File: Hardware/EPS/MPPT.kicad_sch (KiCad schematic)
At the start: 34 parts

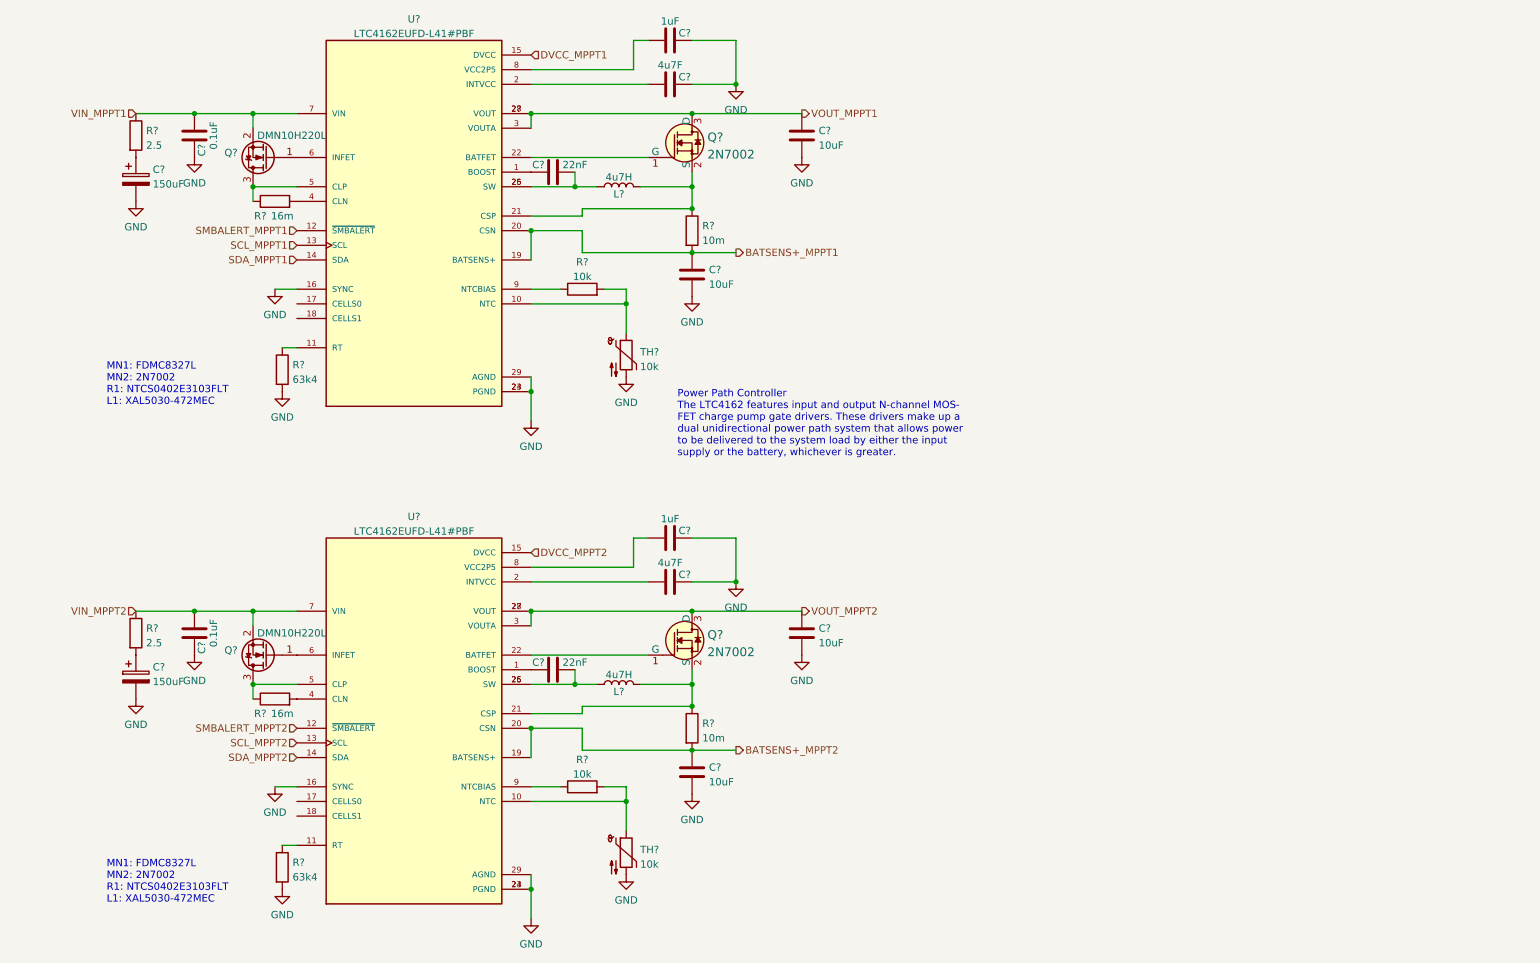
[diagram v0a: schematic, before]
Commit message: Added USB, Solar Connector and MATLAB Folder
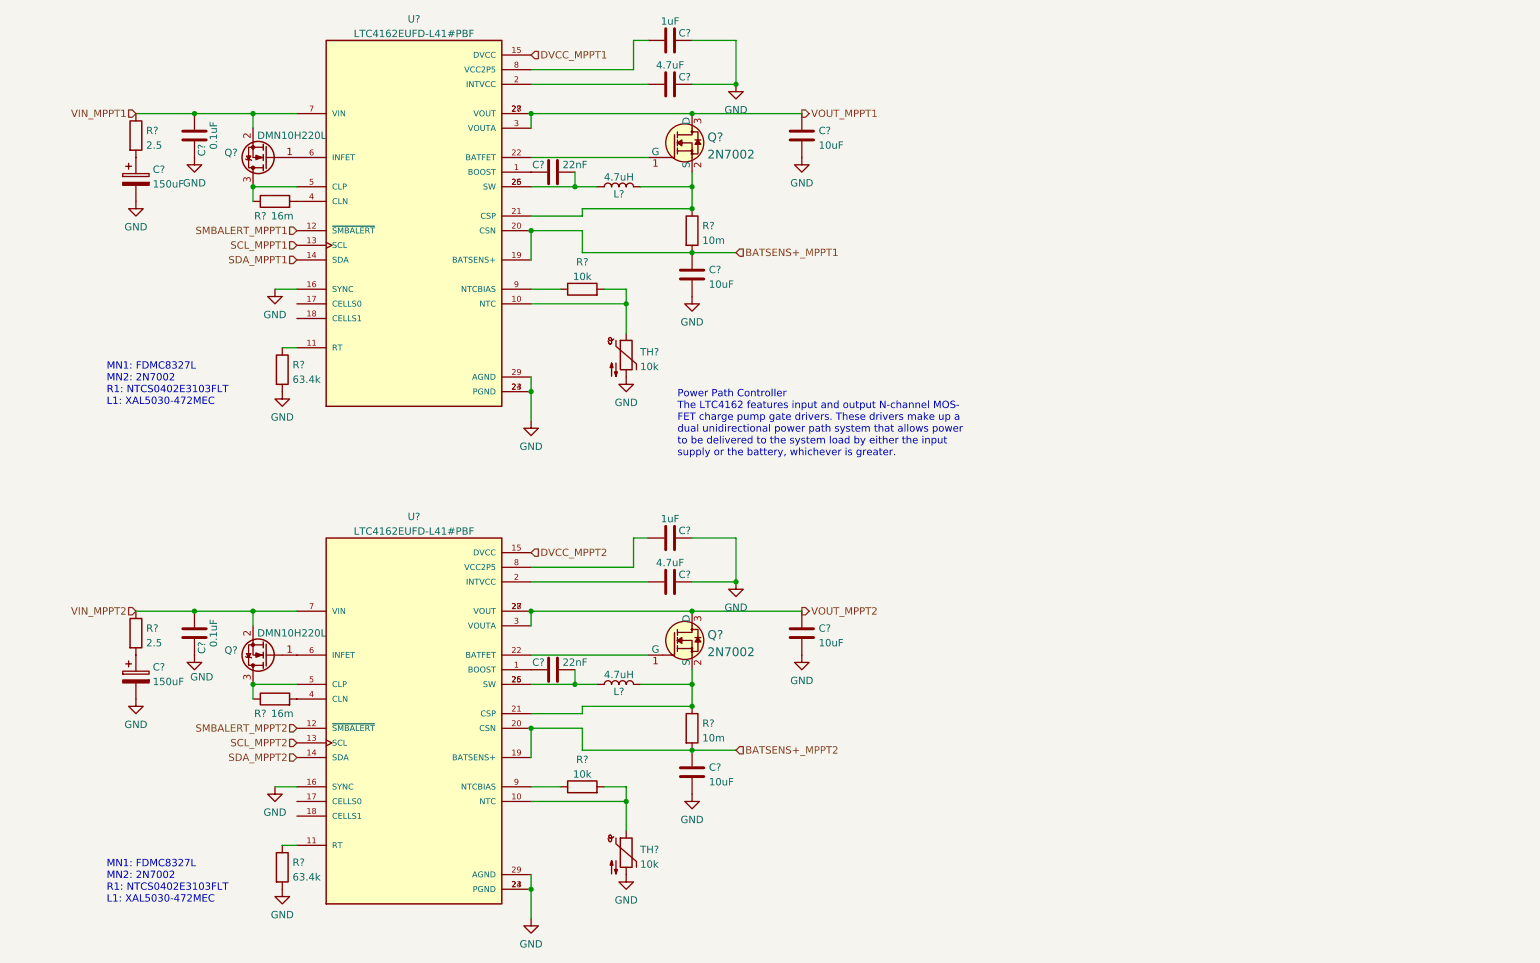
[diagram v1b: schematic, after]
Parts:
- C? (x2): value 4u7F -> 4.7uF
- L? (x2): value 4u7H -> 4.7uH
- R? (x2): value 63k4 -> 63.4k
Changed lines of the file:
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@@
     (effects (font (size 1.27 1.27)) (justify right))
   )
-  (hierarchical_label "BATSENS+_MPPT2" (shape output) (at 144.78 144.78 0)
+  (hierarchical_label "BATSENS+_MPPT2" (shape input) (at 144.78 144.78 0)
     (effects (font (size 1.27 1.27)) (justify left))
   )
@@
     (effects (font (size 1.27 1.27)) (justify right))
   )
-  (hierarchical_label "BATSENS+_MPPT1" (shape output) (at 144.78 58.42 0)
+  (hierarchical_label "BATSENS+_MPPT1" (shape input) (at 144.78 58.42 0)
     (effects (font (size 1.27 1.27)) (justify left))
   )
@@
   )
   (symbol (lib_id "power:GND") (at 50.8 128.27 0) (unit 1)
-    (in_bom yes) (on_board yes) (fields_autoplaced)
+    (in_bom yes) (on_board yes)
     (property "Reference" "#PWR?" (id 0) (at 50.8 134.62 0)
       (effects (font (size 1.27 1.27)) hide)
     )
-    (property "Value" "GND" (id 1) (at 50.8 132.7134 0))
+    (property "Value" "GND" (id 1) (at 52.07 132.08 0))
     (property "Footprint" "" (id 2) (at 50.8 128.27 0)
       (effects (font (size 1.27 1.27)) hide)
@@
     (in_bom yes) (on_board yes)
     (property "Reference" "C?" (id 0) (at 135.89 27.94 90))
-    (property "Value" "4u7F" (id 1) (at 133.35 25.8881 90))
+    (property "Value" "4.7uF" (id 1) (at 133.35 25.8881 90))
     (property "Footprint" "" (id 2) (at 137.16 28.2448 0)
       (effects (font (size 1.27 1.27)) hide)
@@
       (effects (font (size 1.27 1.27)) (justify left))
     )
-    (property "Value" "63k4" (id 1) (at 67.818 166.8022 0)
+    (property "Value" "63.4k" (id 1) (at 67.818 166.8022 0)
       (effects (font (size 1.27 1.27)) (justify left))
     )
@@
       (effects (font (size 1.27 1.27)) (justify left))
     )
-    (property "Value" "63k4" (id 1) (at 67.818 80.4422 0)
+    (property "Value" "63.4k" (id 1) (at 67.818 80.4422 0)
       (effects (font (size 1.27 1.27)) (justify left))
     )
@@
     (in_bom yes) (on_board yes)
     (property "Reference" "L?" (id 0) (at 124.46 134.62 90))
-    (property "Value" "4u7H" (id 1) (at 124.46 131.6791 90))
+    (property "Value" "4.7uH" (id 1) (at 124.46 131.6791 90))
     (property "Footprint" "" (id 2) (at 124.46 133.35 0)
       (effects (font (size 1.27 1.27)) hide)
@@
     (in_bom yes) (on_board yes)
     (property "Reference" "L?" (id 0) (at 124.46 48.26 90))
-    (property "Value" "4u7H" (id 1) (at 124.46 45.3191 90))
+    (property "Value" "4.7uH" (id 1) (at 124.46 45.3191 90))
     (property "Footprint" "" (id 2) (at 124.46 46.99 0)
       (effects (font (size 1.27 1.27)) hide)
@@
     (in_bom yes) (on_board yes)
     (property "Reference" "C?" (id 0) (at 135.89 114.3 90))
-    (property "Value" "4u7F" (id 1) (at 133.35 112.2481 90))
+    (property "Value" "4.7uF" (id 1) (at 133.35 112.2481 90))
     (property "Footprint" "" (id 2) (at 137.16 114.6048 0)
       (effects (font (size 1.27 1.27)) hide)

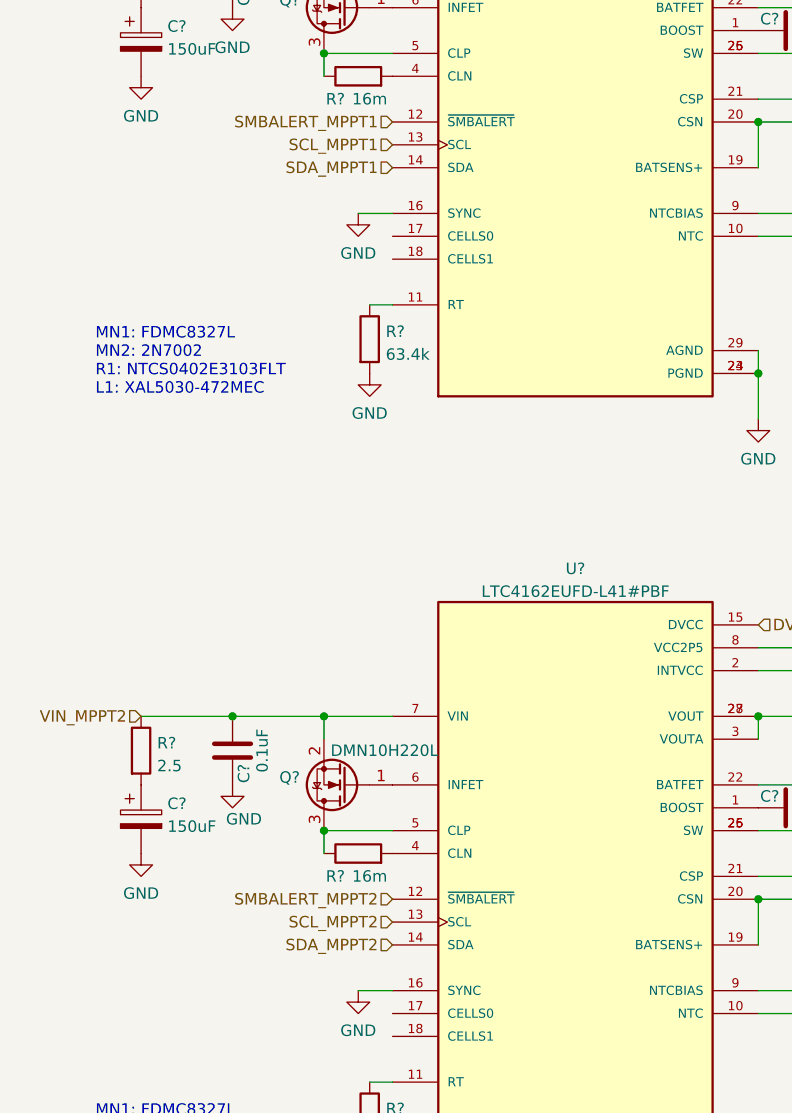
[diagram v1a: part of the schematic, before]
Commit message: Added interboard connector and MCU
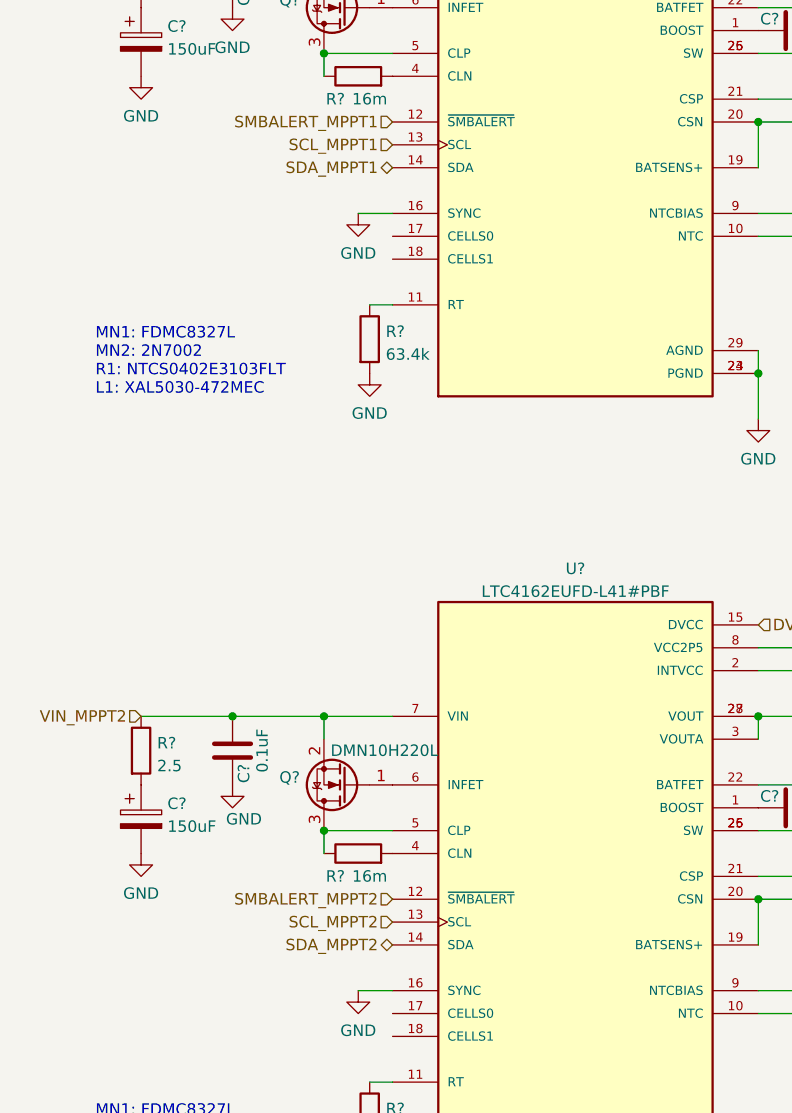
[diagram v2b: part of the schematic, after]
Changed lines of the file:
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@@
     (effects (font (size 1.27 1.27)) (justify left bottom))
   )
-  (hierarchical_label "SDA_MPPT2" (shape input) (at 68.58 146.05 180)
+  (hierarchical_label "SDA_MPPT2" (shape bidirectional) (at 68.58 146.05 180)
     (effects (font (size 1.27 1.27)) (justify right))
   )
@@
     (effects (font (size 1.27 1.27)) (justify right))
   )
-  (hierarchical_label "SDA_MPPT1" (shape input) (at 68.58 59.69 180)
+  (hierarchical_label "SDA_MPPT1" (shape bidirectional) (at 68.58 59.69 180)
     (effects (font (size 1.27 1.27)) (justify right))
   )

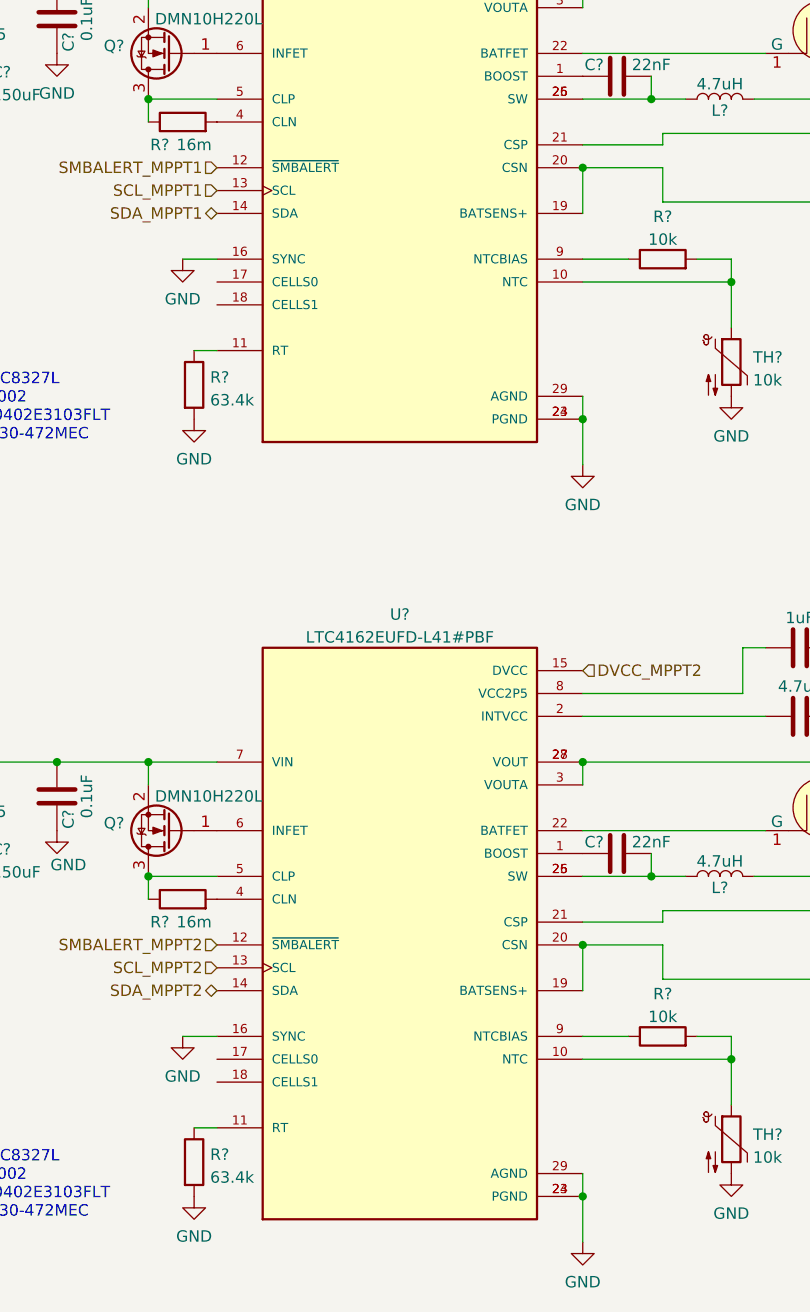
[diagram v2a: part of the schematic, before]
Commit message: Added board connector layout
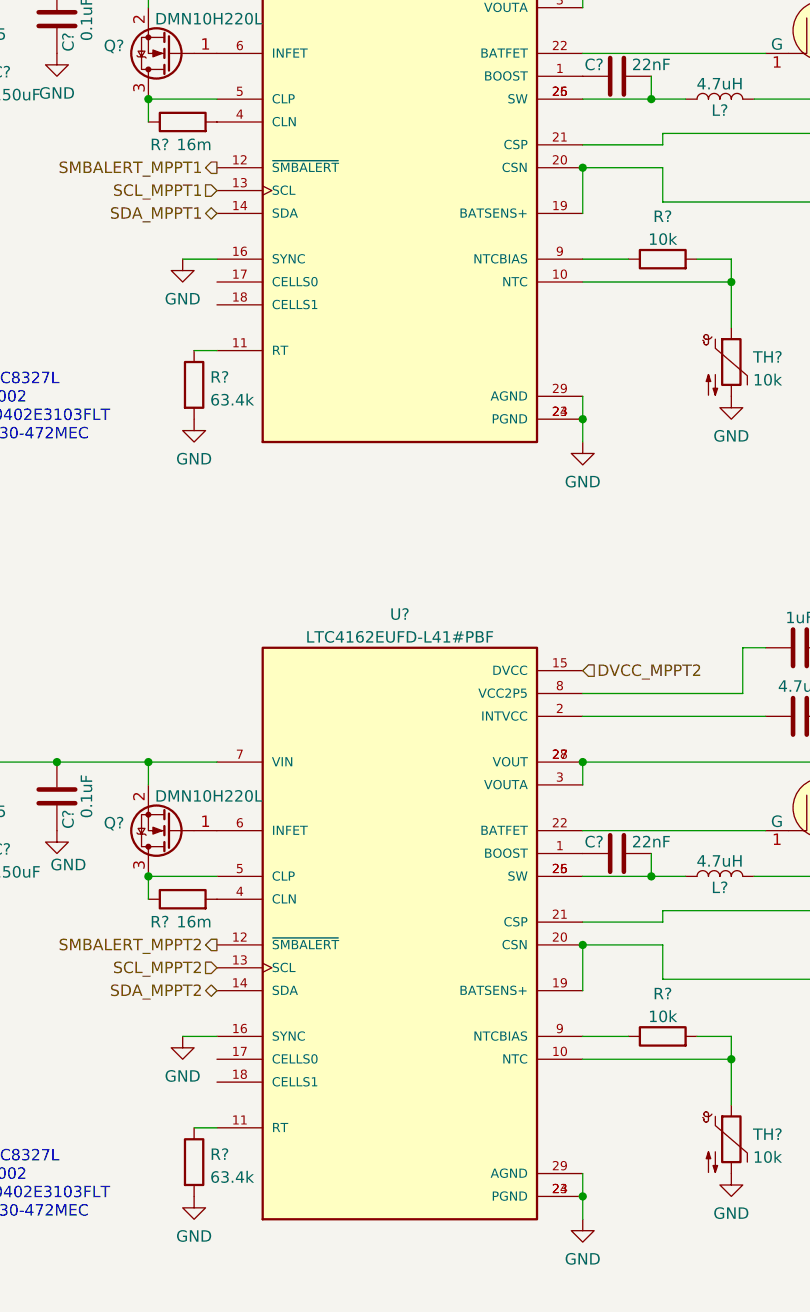
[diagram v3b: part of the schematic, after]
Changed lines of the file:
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@@
     (stroke (width 0) (type default) (color 0 0 0 0))
   )
-  (wire (pts (xy 109.22 82.55) (xy 109.22 87.63))
+  (wire (pts (xy 109.22 82.55) (xy 109.22 85.09))
     (stroke (width 0) (type default) (color 0 0 0 0))
   )
@@
     (stroke (width 0) (type default) (color 0 0 0 0))
   )
-  (wire (pts (xy 109.22 168.91) (xy 109.22 173.99))
+  (wire (pts (xy 109.22 168.91) (xy 109.22 171.45))
     (stroke (width 0) (type default) (color 0 0 0 0))
   )
@@
     (effects (font (size 1.27 1.27)) (justify right))
   )
-  (hierarchical_label "SMBALERT_MPPT1" (shape input) (at 68.58 54.61 180)
+  (hierarchical_label "SMBALERT_MPPT1" (shape output) (at 68.58 54.61 180)
     (effects (font (size 1.27 1.27)) (justify right))
   )
@@
     (effects (font (size 1.27 1.27)) (justify left))
   )
-  (hierarchical_label "SMBALERT_MPPT2" (shape input) (at 68.58 140.97 180)
+  (hierarchical_label "SMBALERT_MPPT2" (shape output) (at 68.58 140.97 180)
     (effects (font (size 1.27 1.27)) (justify right))
   )
@@
     (pin "3")
   )
-  (symbol (lib_id "power:GND") (at 109.22 87.63 0) (unit 1)
-    (in_bom yes) (on_board yes) (fields_autoplaced)
-    (property "Reference" "#PWR?" (id 0) (at 109.22 93.98 0)
-      (effects (font (size 1.27 1.27)) hide)
-    )
-    (property "Value" "GND" (id 1) (at 109.22 92.0734 0))
-    (property "Footprint" "" (id 2) (at 109.22 87.63 0)
-      (effects (font (size 1.27 1.27)) hide)
-    )
-    (property "Datasheet" "" (id 3) (at 109.22 87.63 0)
+  (symbol (lib_id "power:GND") (at 109.22 85.09 0) (unit 1)
+    (in_bom yes) (on_board yes) (fields_autoplaced)
+    (property "Reference" "#PWR?" (id 0) (at 109.22 91.44 0)
+      (effects (font (size 1.27 1.27)) hide)
+    )
+    (property "Value" "GND" (id 1) (at 109.22 89.5334 0))
+    (property "Footprint" "" (id 2) (at 109.22 85.09 0)
+      (effects (font (size 1.27 1.27)) hide)
+    )
+    (property "Datasheet" "" (id 3) (at 109.22 85.09 0)
       (effects (font (size 1.27 1.27)) hide)
     )
@@
     (pin "2")
   )
-  (symbol (lib_id "power:GND") (at 109.22 173.99 0) (unit 1)
-    (in_bom yes) (on_board yes) (fields_autoplaced)
-    (property "Reference" "#PWR?" (id 0) (at 109.22 180.34 0)
-      (effects (font (size 1.27 1.27)) hide)
-    )
-    (property "Value" "GND" (id 1) (at 109.22 178.4334 0))
-    (property "Footprint" "" (id 2) (at 109.22 173.99 0)
-      (effects (font (size 1.27 1.27)) hide)
-    )
-    (property "Datasheet" "" (id 3) (at 109.22 173.99 0)
-      (effects (font (size 1.27 1.27)) hide)
-    )
+  (symbol (lib_id "power:GND") (at 109.22 171.45 0) (unit 1)
+    (in_bom yes) (on_board yes) (fields_autoplaced)
+    (property "Reference" "#PWR?" (id 0) (at 109.22 177.8 0)
+      (effects (font (size 1.27 1.27)) hide)
+    )
+    (property "Value" "GND" (id 1) (at 109.22 175.8934 0))
+    (property "Footprint" "" (id 2) (at 109.22 171.45 0)
+      (effects (font (size 1.27 1.27)) hide)
+    )
+    (property "Datasheet" "" (id 3) (at 109.22 171.45 0)
+      (effects (font (size 1.27 1.27)) hide)
+    )

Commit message: EPS v0.0.1
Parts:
- removed C?: 22nF, symbol Device:C
- removed C?: 150uF, symbol Device:C_Polarized
- removed C? (x2): 10uF, symbol Device:C
- removed C?: 4.7uF, symbol Device:C
- removed C?: 1uF, symbol Device:C
- removed C?: 0.1uF, symbol Device:C
- removed L?: 4.7uH, symbol Device:L
- removed Q?: 2N7002, digikey-footprints:SOT-23-3, symbol dk_Transistors-FETs-MOSFETs-Single:2N7002
- removed Q?: DMN10H220L, Package_TO_SOT_SMD:SOT-23, symbol Transistor_FET:DMN10H220L
- removed R?: 10m, symbol Device:R
- removed R?: 16m, symbol Device:R
- removed R?: 63.4k, symbol Device:R
- removed R?: 10k, symbol Device:R
- removed R?: 2.5, symbol Device:R
- removed TH?: 10k, symbol Device:Thermistor_NTC
- removed U?: LTC4162EUFD-L41#PBF, QFN50P500X400X80-29N, symbol LTC4162EUFD-L41_PBF:LTC4162EUFD-L41#PBF
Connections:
- net SMBALERT_MPPT1 renamed ~{SMBALERT_MPPT1}
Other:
- note added: "A 22nF multi-layer ceramic capacitor is required from SW to BOOST."
- note added: "The compensation capacitor should be a solid or "polymer" electrolytic type such as the Panasonic ZA hybrid series to preserve stable ESR overtemperature. Conventional, or "wet", electrolytic capacitors should be avoided as their ESR increases dramatically at low temperature."
- moved on the sheet: C?, L?, Q?, R?, TH?
